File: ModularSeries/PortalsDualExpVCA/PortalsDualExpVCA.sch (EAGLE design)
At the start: 71 parts, among them IC1 LM13700_DIP, IC2 TL0X4_DIP, IC3 TL0X4_DIP, Q1 2N3906, Q2 2N3906, Q3 2N3906, Q4 2N3906

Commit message: Portals files updated, schematic exports and images included
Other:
- note added: "Ground terminals for jacks / pots"
- note added: "Portals: Dual Exponential VCA Aidan Taylor Spring 2020 ELECTRIC NOODLE BOX Adapted from Ray Wilson's Design: http://musicfromouterspace.com"
- note added: "Unused LM13700 Darlingtons"
- note removed: "Dual Exponential VCA Aidan Taylor Spring 2020 ELECTRIC NOODLE BOX Adapted from Ray Wilson's Design: http://musicfromouterspace.com"
- moved on the sheet: GNDT, H2, H3, H4, IC1B2, POW
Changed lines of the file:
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@@
 <sheet>
 <plain>
-<text x="241.3" y="12.7" size="2.54" layer="91">Dual Exponential VCA
+<text x="241.3" y="12.7" size="2.54" layer="91">Portals: Dual Exponential VCA
 Aidan Taylor Spring 2020
 ELECTRIC NOODLE BOX
 Adapted from Ray Wilson's Design:
 http://musicfromouterspace.com</text>
-<text x="114.3" y="43.18" size="2.54" layer="97">Mounting Holes</text>
+<text x="109.22" y="43.18" size="2.54" layer="97">Mounting Holes</text>
 <text x="15.24" y="40.64" size="2.54" layer="97">Power Decoupling</text>
-<text x="154.94" y="40.64" size="2.54" layer="97">Supply In</text>
+<text x="132.08" y="10.16" size="2.54" layer="97">Supply In</text>
+<text x="73.66" y="17.78" size="1.778" layer="91">Unused LM13700 Darlingtons</text>
+<text x="177.8" y="22.86" size="1.778" layer="91">Ground terminals
+for jacks / pots</text>
 </plain>
 <instances>
@@
 <attribute name="NAME" x="81.28" y="25.4" size="0.6096" layer="95" align="center"/>
 </instance>
-<instance part="IC1" gate="B2" x="99.06" y="27.94" smashed="yes">
-<attribute name="NAME" x="101.6" y="25.4" size="0.6096" layer="95" align="center"/>
+<instance part="IC1" gate="B2" x="93.98" y="27.94" smashed="yes">
+<attribute name="NAME" x="96.52" y="25.4" size="0.6096" layer="95" align="center"/>
 </instance>
 <instance part="IC1" gate="P" x="5.08" y="22.86" smashed="yes">
@@
 </instance>
 <instance part="SO1" gate="G$1" x="129.54" y="63.5" smashed="yes" rot="R180">
-<attribute name="VALUE" x="132.08" y="68.326" size="1.778" layer="96" font="vector" rot="R180"/>
 <attribute name="NAME" x="132.08" y="60.452" size="1.778" layer="95" font="vector" rot="R180"/>
 </instance>
@@
 <attribute name="NAME" x="113.792" y="38.6842" size="1.778" layer="95"/>
 </instance>
-<instance part="H2" gate="G$1" x="119.38" y="38.1" smashed="yes">
-<attribute name="NAME" x="121.412" y="38.6842" size="1.778" layer="95"/>
-</instance>
-<instance part="H3" gate="G$1" x="127" y="38.1" smashed="yes">
-<attribute name="NAME" x="129.032" y="38.6842" size="1.778" layer="95"/>
-</instance>
-<instance part="H4" gate="G$1" x="134.62" y="38.1" smashed="yes">
-<attribute name="NAME" x="136.652" y="38.6842" size="1.778" layer="95"/>
-</instance>
-<instance part="POW" gate="G$1" x="157.48" y="27.94" smashed="yes" rot="MR180">
-<attribute name="NAME" x="152.4" y="19.812" size="1.778" layer="95" font="vector" rot="MR180"/>
-</instance>
-<instance part="P+6" gate="1" x="165.1" y="35.56" smashed="yes">
-<attribute name="VALUE" x="162.56" y="30.48" size="1.778" layer="96" rot="R90"/>
-</instance>
-<instance part="P-6" gate="1" x="165.1" y="17.78" smashed="yes">
-<attribute name="VALUE" x="162.56" y="15.24" size="1.778" layer="96" rot="R90"/>
-</instance>
-<instance part="AGND17" gate="VR1" x="172.72" y="20.32" smashed="yes">
-<attribute name="VALUE" x="170.18" y="15.24" size="1.778" layer="96" rot="R90"/>
+<instance part="H2" gate="G$1" x="111.76" y="33.02" smashed="yes">
+<attribute name="NAME" x="113.792" y="33.6042" size="1.778" layer="95"/>
+</instance>
+<instance part="H3" gate="G$1" x="111.76" y="27.94" smashed="yes">
+<attribute name="NAME" x="113.792" y="28.5242" size="1.778" layer="95"/>
+</instance>
+<instance part="H4" gate="G$1" x="111.76" y="22.86" smashed="yes">
+<attribute name="NAME" x="113.792" y="23.4442" size="1.778" layer="95"/>
+</instance>
+<instance part="POW" gate="G$1" x="134.62" y="27.94" smashed="yes" rot="MR180">
+<attribute name="NAME" x="129.54" y="19.812" size="1.778" layer="95" font="vector" rot="MR180"/>
+</instance>
+<instance part="P+6" gate="1" x="142.24" y="35.56" smashed="yes">
+<attribute name="VALUE" x="139.7" y="30.48" size="1.778" layer="96" rot="R90"/>
+</instance>
+<instance part="P-6" gate="1" x="142.24" y="17.78" smashed="yes">
+<attribute name="VALUE" x="139.7" y="15.24" size="1.778" layer="96" rot="R90"/>
+</instance>
+<instance part="AGND17" gate="VR1" x="149.86" y="20.32" smashed="yes">
+<attribute name="VALUE" x="147.32" y="15.24" size="1.778" layer="96" rot="R90"/>
 </instance>
 <instance part="INV1" gate="G$1" x="7.62" y="73.66" smashed="yes">
@@
 <attribute name="VALUE" x="171.45" y="70.358" size="1.778" layer="96"/>
 </instance>
-<instance part="GNDT" gate="G$1" x="190.5" y="25.4" smashed="yes">
-<attribute name="NAME" x="185.42" y="33.528" size="1.778" layer="95" font="vector"/>
-</instance>
-<instance part="AGND16" gate="VR1" x="198.12" y="17.78" smashed="yes">
-<attribute name="VALUE" x="195.58" y="12.7" size="1.778" layer="96" rot="R90"/>
+<instance part="GNDT" gate="G$1" x="165.1" y="25.4" smashed="yes">
+<attribute name="NAME" x="160.02" y="33.528" size="1.778" layer="95" font="vector"/>
+</instance>
+<instance part="AGND16" gate="VR1" x="172.72" y="17.78" smashed="yes">
+<attribute name="VALUE" x="170.18" y="12.7" size="1.778" layer="96" rot="R90"/>
 </instance>
 <instance part="BIAS1" gate="G$1" x="7.62" y="111.76" smashed="yes">
@@
 <segment>
 <pinref part="AGND17" gate="VR1" pin="AGND"/>
+<wire x1="149.86" y1="27.94" x2="149.86" y2="25.4" width="0.1524" layer="91"/>
+<pinref part="POW" gate="G$1" pin="3"/>
+<wire x1="149.86" y1="25.4" x2="149.86" y2="22.86" width="0.1524" layer="91"/>
+<wire x1="139.7" y1="25.4" x2="149.86" y2="25.4" width="0.1524" layer="91"/>
+<junction x="149.86" y="25.4"/>
+<pinref part="POW" gate="G$1" pin="2"/>
+<wire x1="139.7" y1="27.94" x2="149.86" y2="27.94" width="0.1524" layer="91"/>
+</segment>
+<segment>
+<pinref part="GNDT" gate="G$1" pin="4"/>
+<wire x1="170.18" y1="30.48" x2="172.72" y2="30.48" width="0.1524" layer="91"/>
+<pinref part="AGND16" gate="VR1" pin="AGND"/>
+<wire x1="172.72" y1="30.48" x2="172.72" y2="27.94" width="0.1524" layer="91"/>
+<pinref part="GNDT" gate="G$1" pin="3"/>
 <wire x1="172.72" y1="27.94" x2="172.72" y2="25.4" width="0.1524" layer="91"/>
-<pinref part="POW" gate="G$1" pin="3"/>
 <wire x1="172.72" y1="25.4" x2="172.72" y2="22.86" width="0.1524" layer="91"/>
-<wire x1="162.56" y1="25.4" x2="172.72" y2="25.4" width="0.1524" layer="91"/>
+<wire x1="172.72" y1="22.86" x2="172.72" y2="20.32" width="0.1524" layer="91"/>
+<wire x1="170.18" y1="27.94" x2="172.72" y2="27.94" width="0.1524" layer="91"/>
+<junction x="172.72" y="27.94"/>
+<pinref part="GNDT" gate="G$1" pin="2"/>
+<wire x1="170.18" y1="25.4" x2="172.72" y2="25.4" width="0.1524" layer="91"/>
 <junction x="172.72" y="25.4"/>
-<pinref part="POW" gate="G$1" pin="2"/>
-<wire x1="162.56" y1="27.94" x2="172.72" y2="27.94" width="0.1524" layer="91"/>
-</segment>
-<segment>
-<pinref part="GNDT" gate="G$1" pin="4"/>
-<wire x1="195.58" y1="30.48" x2="198.12" y2="30.48" width="0.1524" layer="91"/>
-<pinref part="AGND16" gate="VR1" pin="AGND"/>
-<wire x1="198.12" y1="30.48" x2="198.12" y2="27.94" width="0.1524" layer="91"/>
-<pinref part="GNDT" gate="G$1" pin="3"/>
-<wire x1="198.12" y1="27.94" x2="198.12" y2="25.4" width="0.1524" layer="91"/>
-<wire x1="198.12" y1="25.4" x2="198.12" y2="22.86" width="0.1524" layer="91"/>
-<wire x1="198.12" y1="22.86" x2="198.12" y2="20.32" width="0.1524" layer="91"/>
-<wire x1="195.58" y1="27.94" x2="198.12" y2="27.94" width="0.1524" layer="91"/>
-<junction x="198.12" y="27.94"/>
-<pinref part="GNDT" gate="G$1" pin="2"/>
-<wire x1="195.58" y1="25.4" x2="198.12" y2="25.4" width="0.1524" layer="91"/>
-<junction x="198.12" y="25.4"/>
 <pinref part="GNDT" gate="G$1" pin="1"/>
-<wire x1="195.58" y1="22.86" x2="198.12" y2="22.86" width="0.1524" layer="91"/>
-<junction x="198.12" y="22.86"/>
+<wire x1="170.18" y1="22.86" x2="172.72" y2="22.86" width="0.1524" layer="91"/>
+<junction x="172.72" y="22.86"/>
 </segment>
 </net>
@@
 <segment>
 <pinref part="P+6" gate="1" pin="+12V"/>
-<wire x1="165.1" y1="30.48" x2="165.1" y2="33.02" width="0.1524" layer="91"/>
+<wire x1="142.24" y1="30.48" x2="142.24" y2="33.02" width="0.1524" layer="91"/>
 <pinref part="POW" gate="G$1" pin="1"/>
-<wire x1="165.1" y1="30.48" x2="162.56" y2="30.48" width="0.1524" layer="91"/>
+<wire x1="142.24" y1="30.48" x2="139.7" y2="30.48" width="0.1524" layer="91"/>
 </segment>
 </net>
@@
 <segment>
 <pinref part="P-6" gate="1" pin="-12V"/>
-<wire x1="165.1" y1="22.86" x2="165.1" y2="20.32" width="0.1524" layer="91"/>
+<wire x1="142.24" y1="22.86" x2="142.24" y2="20.32" width="0.1524" layer="91"/>
 <pinref part="POW" gate="G$1" pin="4"/>
-<wire x1="165.1" y1="22.86" x2="162.56" y2="22.86" width="0.1524" layer="91"/>
-</segment>
-</net>
+<wire x1="142.24" y1="22.86" x2="139.7" y2="22.86" width="0.1524" layer="91"/>
+</segment>
+</net>

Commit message: Library updated, variants consolidated
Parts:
- IC1: value LM13700_DIP -> (none); device ElectricNoodleBox:LM13700_DIP -> ElectricNoodleBox:LM13700DIL
- IC2, IC3: value TL0X4_DIP -> (none); device ElectricNoodleBox:TL0X4_DIP -> ElectricNoodleBox:TL0X4DIL
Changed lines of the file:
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@@
 </classes>
 <parts>
-<part name="IC1" library="ElectricNoodleBox" deviceset="LM13700_DIP" device="" package3d_urn="urn:adsk.eagle:package:922/2"/>
+<part name="IC1" library="ElectricNoodleBox" deviceset="LM13700" device="DIL" package3d_urn="urn:adsk.eagle:package:922/2"/>
 <part name="SI1" library="ElectricNoodleBox" deviceset="1XWIREPAD" device=""/>
 <part name="R1" library="rcl" library_urn="urn:adsk.eagle:library:334" deviceset="R-EU_" device="0207/10" package3d_urn="urn:adsk.eagle:package:23491/2" value="22K"/>
@@
 <part name="R4" library="rcl" library_urn="urn:adsk.eagle:library:334" deviceset="R-EU_" device="0207/10" package3d_urn="urn:adsk.eagle:package:23491/2" value="1K"/>
 <part name="R5" library="rcl" library_urn="urn:adsk.eagle:library:334" deviceset="R-EU_" device="0207/10" package3d_urn="urn:adsk.eagle:package:23491/2" value="33K"/>
-<part name="IC2" library="ElectricNoodleBox" deviceset="TL0X4_DIP" device="" package3d_urn="urn:adsk.eagle:package:16407/2"/>
+<part name="IC2" library="ElectricNoodleBox" deviceset="TL0X4" device="DIL" package3d_urn="urn:adsk.eagle:package:16407/2"/>
 <part name="P+1" library="supply1" library_urn="urn:adsk.eagle:library:371" deviceset="+12V" device=""/>
 <part name="P-1" library="supply1" library_urn="urn:adsk.eagle:library:371" deviceset="-12V" device=""/>
@@
 <part name="R21" library="rcl" library_urn="urn:adsk.eagle:library:334" deviceset="R-EU_" device="0207/10" package3d_urn="urn:adsk.eagle:package:23491/2" value="1K"/>
 <part name="R22" library="rcl" library_urn="urn:adsk.eagle:library:334" deviceset="R-EU_" device="0207/10" package3d_urn="urn:adsk.eagle:package:23491/2" value="33K"/>
-<part name="IC3" library="ElectricNoodleBox" deviceset="TL0X4_DIP" device="" package3d_urn="urn:adsk.eagle:package:16407/2"/>
+<part name="IC3" library="ElectricNoodleBox" deviceset="TL0X4" device="DIL" package3d_urn="urn:adsk.eagle:package:16407/2"/>
 <part name="C3" library="rcl" library_urn="urn:adsk.eagle:library:334" deviceset="C-EU" device="050-025X075" package3d_urn="urn:adsk.eagle:package:23637/1" value="22pF"/>
 <part name="R23" library="rcl" library_urn="urn:adsk.eagle:library:334" deviceset="R-EU_" device="0207/10" package3d_urn="urn:adsk.eagle:package:23491/2" value="75K"/>

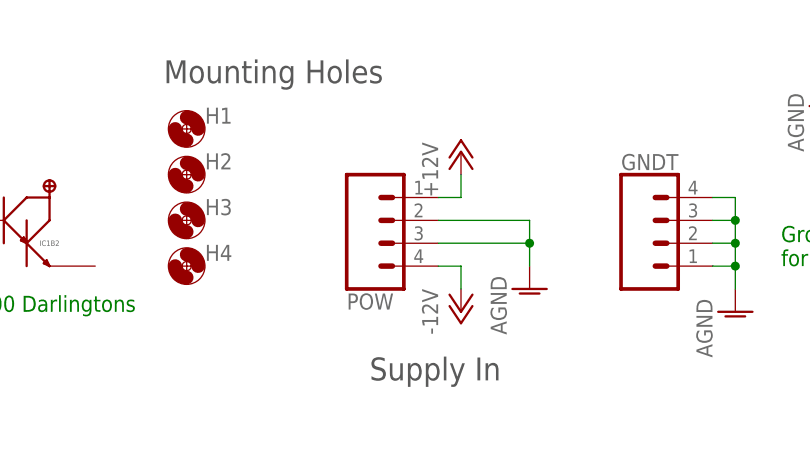
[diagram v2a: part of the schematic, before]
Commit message: Power header updated on most PCBs. Knives layout added
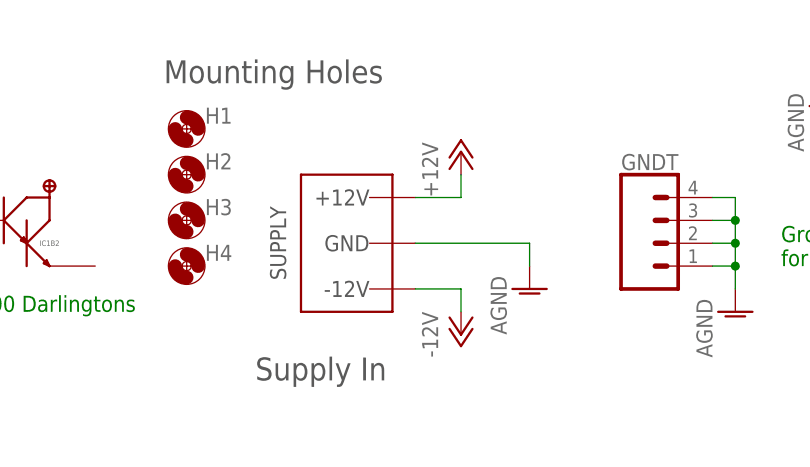
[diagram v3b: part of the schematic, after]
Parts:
- removed POW: 4XMOLEX, ElectricNoodleBox:4XMOLEX
- added WP1: COMBO_SUPPLY_HEADER, ElectricNoodleBox:COMBO_SUPPLY_HEADER
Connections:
- net +12V: now also WP1.V++; no longer POW.1
- net -12V: now also WP1.V--; no longer POW.4
- net AGND: now also WP1.AGND; no longer POW.2, POW.3
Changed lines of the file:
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@@
 <part name="H3" library="holes" library_urn="urn:adsk.eagle:library:237" deviceset="MOUNT-HOLE" device="3.2" package3d_urn="urn:adsk.eagle:package:14275/1"/>
 <part name="H4" library="holes" library_urn="urn:adsk.eagle:library:237" deviceset="MOUNT-HOLE" device="3.2" package3d_urn="urn:adsk.eagle:package:14275/1"/>
-<part name="POW" library="ElectricNoodleBox" deviceset="4XMOLEX" device=""/>
 <part name="P+6" library="supply1" library_urn="urn:adsk.eagle:library:371" deviceset="+12V" device=""/>
 <part name="P-6" library="supply1" library_urn="urn:adsk.eagle:library:371" deviceset="-12V" device=""/>
@@
 <part name="BIAS1" library="ElectricNoodleBox" deviceset="3XWIREPAD" device=""/>
 <part name="BIAS2" library="ElectricNoodleBox" deviceset="3XWIREPAD" device=""/>
+<part name="WP1" library="ElectricNoodleBox" deviceset="COMBO_SUPPLY_HEADER" device=""/>
 </parts>
 <sheets>
@@
 <text x="109.22" y="43.18" size="2.54" layer="97">Mounting Holes</text>
 <text x="15.24" y="40.64" size="2.54" layer="97">Power Decoupling</text>
-<text x="132.08" y="10.16" size="2.54" layer="97">Supply In</text>
+<text x="119.38" y="10.16" size="2.54" layer="97">Supply In</text>
 <text x="73.66" y="17.78" size="1.778" layer="91">Unused LM13700 Darlingtons</text>
 <text x="177.8" y="22.86" size="1.778" layer="91">Ground terminals
@@
 <attribute name="NAME" x="113.792" y="23.4442" size="1.778" layer="95"/>
 </instance>
-<instance part="POW" gate="G$1" x="134.62" y="27.94" smashed="yes" rot="MR180">
-<attribute name="NAME" x="129.54" y="19.812" size="1.778" layer="95" font="vector" rot="MR180"/>
-</instance>
 <instance part="P+6" gate="1" x="142.24" y="35.56" smashed="yes">
 <attribute name="VALUE" x="139.7" y="30.48" size="1.778" layer="96" rot="R90"/>
 </instance>
-<instance part="P-6" gate="1" x="142.24" y="17.78" smashed="yes">
-<attribute name="VALUE" x="139.7" y="15.24" size="1.778" layer="96" rot="R90"/>
+<instance part="P-6" gate="1" x="142.24" y="15.24" smashed="yes">
+<attribute name="VALUE" x="139.7" y="12.7" size="1.778" layer="96" rot="R90"/>
 </instance>
 <instance part="AGND17" gate="VR1" x="149.86" y="20.32" smashed="yes">
@@
 <attribute name="NAME" x="157.48" y="117.348" size="1.778" layer="95" font="vector"/>
 </instance>
+<instance part="WP1" gate="G$1" x="129.54" y="25.4" smashed="yes" rot="MR0"/>
 </instances>
 <busses>
@@
 <segment>
 <pinref part="AGND17" gate="VR1" pin="AGND"/>
-<wire x1="149.86" y1="27.94" x2="149.86" y2="25.4" width="0.1524" layer="91"/>
-<pinref part="POW" gate="G$1" pin="3"/>
 <wire x1="149.86" y1="25.4" x2="149.86" y2="22.86" width="0.1524" layer="91"/>
-<wire x1="139.7" y1="25.4" x2="149.86" y2="25.4" width="0.1524" layer="91"/>
-<junction x="149.86" y="25.4"/>
-<pinref part="POW" gate="G$1" pin="2"/>
-<wire x1="139.7" y1="27.94" x2="149.86" y2="27.94" width="0.1524" layer="91"/>
+<wire x1="137.16" y1="25.4" x2="149.86" y2="25.4" width="0.1524" layer="91"/>
+<pinref part="WP1" gate="G$1" pin="AGND"/>
 </segment>
 <segment>
@@
 <pinref part="P+6" gate="1" pin="+12V"/>
 <wire x1="142.24" y1="30.48" x2="142.24" y2="33.02" width="0.1524" layer="91"/>
-<pinref part="POW" gate="G$1" pin="1"/>
-<wire x1="142.24" y1="30.48" x2="139.7" y2="30.48" width="0.1524" layer="91"/>
+<pinref part="WP1" gate="G$1" pin="V++"/>
+<wire x1="137.16" y1="30.48" x2="142.24" y2="30.48" width="0.1524" layer="91"/>
 </segment>
 </net>
@@
 <segment>
 <pinref part="P-6" gate="1" pin="-12V"/>
-<wire x1="142.24" y1="22.86" x2="142.24" y2="20.32" width="0.1524" layer="91"/>
-<pinref part="POW" gate="G$1" pin="4"/>
-<wire x1="142.24" y1="22.86" x2="139.7" y2="22.86" width="0.1524" layer="91"/>
-</segment>
-</net>
+<wire x1="142.24" y1="20.32" x2="142.24" y2="17.78" width="0.1524" layer="91"/>
+<pinref part="WP1" gate="G$1" pin="V--"/>
+<wire x1="137.16" y1="20.32" x2="142.24" y2="20.32" width="0.1524" layer="91"/>
+</segment>
+</net>
